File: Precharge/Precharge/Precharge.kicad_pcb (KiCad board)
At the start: 2 copper layers, 133 x 98 mm, 121 parts, among them J1 MicroFit, J2 Mini-Fit_Jr_5566-04A, J3 Micro-Fit 43045-0212, K1 OMRON-G2RL-24, K2 G7L-2A-X-L, Q1 2N7002, Q2 MMBT3906, Q3 2N7002, U1 TJA1051T-3, U10 LM393, U11 4N35, U2 SPAN02A-12, U3 Teensy4.0, U4 LM1117-5.0, U5 4N35, U6 4N35, U7 LM331, U8 LM331, U9 LM2904

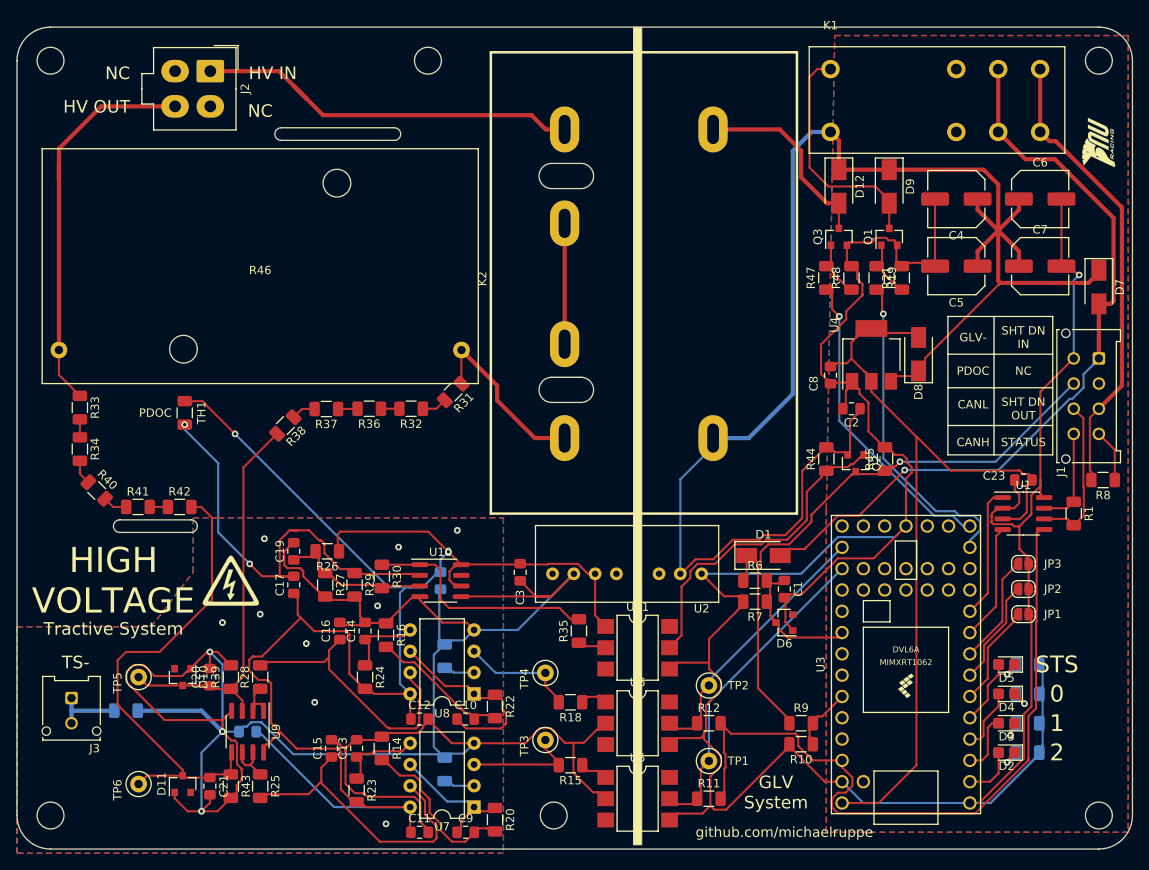
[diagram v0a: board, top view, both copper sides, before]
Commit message: :pencil: tidy-up pcb artwork
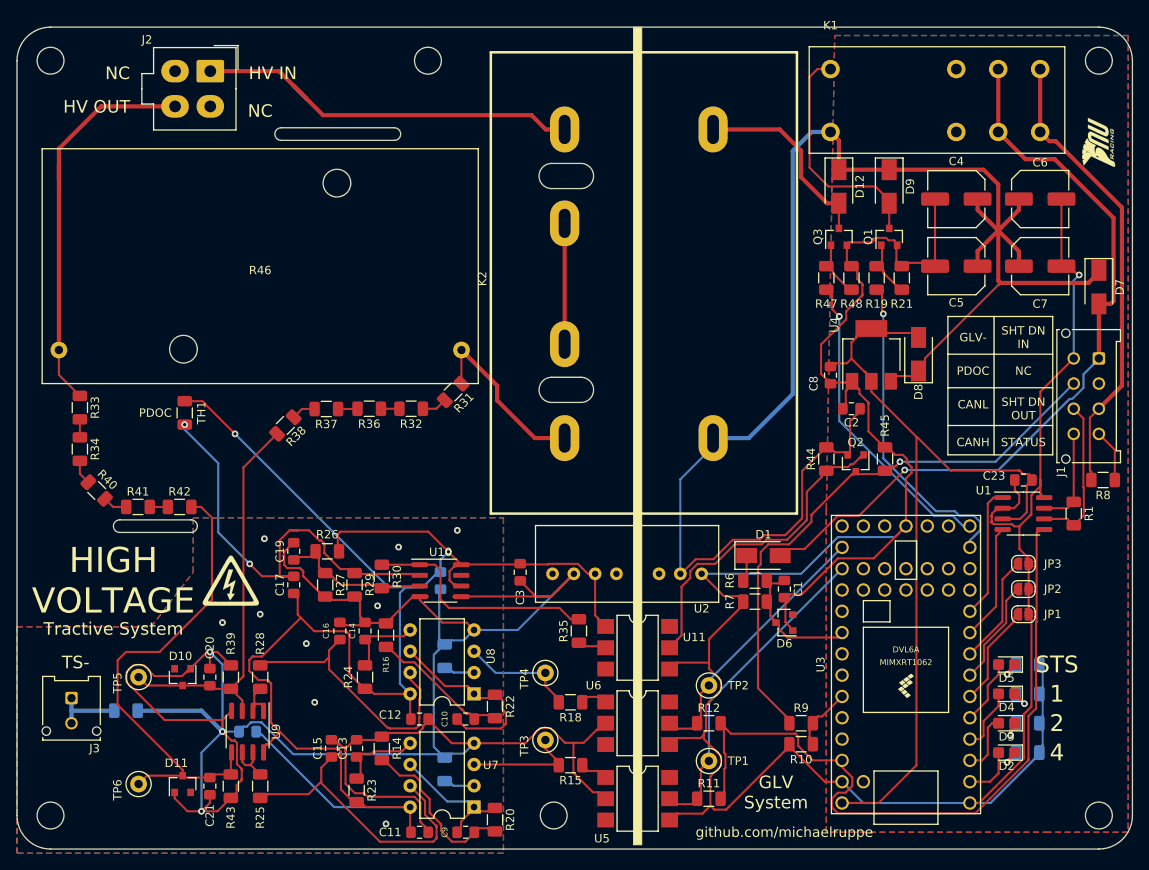
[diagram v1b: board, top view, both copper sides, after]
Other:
- board text added: "4"
- board text removed: "0"
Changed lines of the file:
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@@
       (outputformat 1)
       (mirror false)
-      (drillshape 1)
+      (drillshape 0)
       (scaleselection 1)
-      (outputdirectory ""))
+      (outputdirectory "C:/Users/Michael/Desktop/precharge-gerbers/"))
   )
   (net 0 "")
@@
     (descr "Molex Mini-Fit Jr. Power Connectors, old mpn/engineering number: 5566-04A, example for new mpn: 39-28-x04x, 2 Pins per row, Mounting:  (http://www.molex.com/pdm_docs/sd/039281043_sd.pdf), generated with kicad-footprint-generator")
     (tags "connector Molex Mini-Fit_Jr side entry")
-    (fp_text reference J2 (at 2.1 -3.45 90) (layer F.SilkS)
+    (fp_text reference J2 (at -3.75 8.25 180) (layer F.SilkS)
       (effects (font (size 1 1) (thickness 0.15)))
     )
@@
     (tags "SOIC SO")
     (attr smd)
-    (fp_text reference U1 (at 0 -3.4) (layer F.SilkS)
+    (fp_text reference U1 (at -4.75 -2.75) (layer F.SilkS)
       (effects (font (size 1 1) (thickness 0.15)))
     )
@@
     (tags "SMD DIP DIL PDIP SMDIP 2.54mm 7.62mm 300mil")
     (attr smd)
-    (fp_text reference U11 (at 0 -4.87) (layer F.SilkS)
+    (fp_text reference U11 (at 6.75 -1.25) (layer F.SilkS)
       (effects (font (size 1 1) (thickness 0.15)))
     )
@@
     (tags "SMD DIP DIL PDIP SMDIP 2.54mm 7.62mm 300mil")
     (attr smd)
-    (fp_text reference U6 (at 0 -4.87) (layer F.SilkS)
+    (fp_text reference U6 (at -5.25 -4.5) (layer F.SilkS)
       (effects (font (size 1 1) (thickness 0.15)))
     )
@@
     (tags "SMD DIP DIL PDIP SMDIP 2.54mm 7.62mm 300mil")
     (attr smd)
-    (fp_text reference U5 (at 0 -4.87) (layer F.SilkS)
+    (fp_text reference U5 (at -4.25 4.75) (layer F.SilkS)
       (effects (font (size 1 1) (thickness 0.15)))
     )
@@
     (descr "8-lead though-hole mounted DIP package, row spacing 7.62 mm (300 mils)")
     (tags "THT DIP DIL PDIP 2.54mm 7.62mm 300mil")
-    (fp_text reference U8 (at 3.81 -2.33) (layer F.SilkS)
+    (fp_text reference U8 (at -2 4.5 90) (layer F.SilkS)
       (effects (font (size 1 1) (thickness 0.15)))
     )
@@
     (descr "8-lead though-hole mounted DIP package, row spacing 7.62 mm (300 mils)")
     (tags "THT DIP DIL PDIP 2.54mm 7.62mm 300mil")
-    (fp_text reference U7 (at 3.81 -2.33) (layer F.SilkS)
+    (fp_text reference U7 (at -2 5) (layer F.SilkS)
       (effects (font (size 1 1) (thickness 0.15)))
     )
@@
     (tags resistor)
     (attr smd)
-    (fp_text reference R45 (at 0 -1.82 90) (layer F.SilkS)
+    (fp_text reference R45 (at 4 0 90) (layer F.SilkS)
       (effects (font (size 1 1) (thickness 0.15)))
     )
@@
     (tags resistor)
     (attr smd)
-    (fp_text reference R43 (at 0 -1.82 90) (layer F.SilkS)
+    (fp_text reference R43 (at 3.75 0 90) (layer F.SilkS)
       (effects (font (size 1 1) (thickness 0.15)))
     )
@@
     (tags resistor)
     (attr smd)
-    (fp_text reference R39 (at 0 -1.82 90) (layer F.SilkS)
+    (fp_text reference R39 (at 4 0 90) (layer F.SilkS)
       (effects (font (size 1 1) (thickness 0.15)))
     )
@@
     (tags resistor)
     (attr smd)
-    (fp_text reference R28 (at 0 -1.82 90) (layer F.SilkS)
+    (fp_text reference R28 (at 4 0 90) (layer F.SilkS)
       (effects (font (size 1 1) (thickness 0.15)))
     )
@@
     (tags resistor)
     (attr smd)
-    (fp_text reference R25 (at 0 -1.82 90) (layer F.SilkS)
+    (fp_text reference R25 (at 3.75 0 90) (layer F.SilkS)
       (effects (font (size 1 1) (thickness 0.15)))
     )
@@
     (tags resistor)
     (attr smd)
-    (fp_text reference R24 (at 0 -1.82 90) (layer F.SilkS)
+    (fp_text reference R24 (at 0 2 90) (layer F.SilkS)
       (effects (font (size 1 1) (thickness 0.15)))
     )
@@
     (tags resistor)
     (attr smd)
-    (fp_text reference R16 (at 0 -1.82 90) (layer F.SilkS)
-      (effects (font (size 1 1) (thickness 0.15)))
+    (fp_text reference R16 (at 3.5 0 90) (layer F.SilkS)
+      (effects (font (size 0.7 0.7) (thickness 0.15)))
     )
     (fp_text value 47 (at 0 1.82 90) (layer F.Fab)
@@
     (tags resistor)
     (attr smd)
-    (fp_text reference R7 (at 0 -1.82) (layer F.SilkS)
+    (fp_text reference R7 (at 3 0 90) (layer F.SilkS)
       (effects (font (size 1 1) (thickness 0.15)))
     )
@@
     (tags resistor)
     (attr smd)
-    (fp_text reference R6 (at 0 -1.82) (layer F.SilkS)
+    (fp_text reference R6 (at -3 0 90) (layer F.SilkS)
       (effects (font (size 1 1) (thickness 0.15)))
     )
@@
     (tags SOT-23)
     (attr smd)
-    (fp_text reference Q2 (at 0 -2.5 90) (layer F.SilkS)
+    (fp_text reference Q2 (at -2.5 0 180) (layer F.SilkS)
       (effects (font (size 1 1) (thickness 0.15)))
     )
@@
     (tags SOT-23)
     (attr smd)
-    (fp_text reference D11 (at 0 -2.5 90) (layer F.SilkS)
+    (fp_text reference D11 (at 2.5 -0.75 180) (layer F.SilkS)
       (effects (font (size 1 1) (thickness 0.15)))
     )
@@
     (tags SOT-23)
     (attr smd)
-    (fp_text reference D10 (at 0 -2.5 90) (layer F.SilkS)
+    (fp_text reference D10 (at -2.5 0.25 180) (layer F.SilkS)
       (effects (font (size 1 1) (thickness 0.15)))
     )
@@
     (tags "capacitor electrolyic nonpolar")
     (attr smd)
-    (fp_text reference C7 (at 0 -4.35) (layer F.SilkS)
+    (fp_text reference C7 (at 0 4.5) (layer F.SilkS)
       (effects (font (size 1 1) (thickness 0.15)))
     )
@@
     (tags "capacitor handsolder")
     (attr smd)
-    (fp_text reference C21 (at 0 -1.65 90) (layer F.SilkS)
+    (fp_text reference C21 (at 3.5 0 90) (layer F.SilkS)
       (effects (font (size 1 1) (thickness 0.15)))
     )
@@
     (tags "capacitor handsolder")
     (attr smd)
-    (fp_text reference C20 (at 0 -1.65 90) (layer F.SilkS)
+    (fp_text reference C20 (at 3.5 0 90) (layer F.SilkS)
       (effects (font (size 1 1) (thickness 0.15)))
     )
@@
     (attr smd)
     (fp_text reference C16 (at 0 -1.65 90) (layer F.SilkS)
-      (effects (font (size 1 1) (thickness 0.15)))
+      (effects (font (size 0.7 0.7) (thickness 0.15)))
     )
     (fp_text value 100n (at 0 1.65 90) (layer F.Fab)
@@
     (tags "capacitor handsolder")
     (attr smd)
-    (fp_text reference C14 (at 0 -1.65 90) (layer F.SilkS)
-      (effects (font (size 1 1) (thickness 0.15)))
+    (fp_text reference C14 (at 0 -1.5 90) (layer F.SilkS)
+      (effects (font (size 0.7 0.7) (thickness 0.15)))
     )
     (fp_text value 10n (at 0 1.65 90) (layer F.Fab)
@@
     (tags "capacitor handsolder")
     (attr smd)
-    (fp_text reference C12 (at 0 -1.65) (layer F.SilkS)
+    (fp_text reference C12 (at -3.5 -0.5) (layer F.SilkS)
       (effects (font (size 1 1) (thickness 0.15)))
     )
@@
     (tags "capacitor handsolder")
     (attr smd)
-    (fp_text reference C11 (at 0 -1.65) (layer F.SilkS)
+    (fp_text reference C11 (at -3.5 0) (layer F.SilkS)
       (effects (font (size 1 1) (thickness 0.15)))
     )
@@
     (tags "capacitor handsolder")
     (attr smd)
-    (fp_text reference C10 (at 0 -1.65) (layer F.SilkS)
-      (effects (font (size 1 1) (thickness 0.15)))
+    (fp_text reference C10 (at -2.5 0 90) (layer F.SilkS)
+      (effects (font (size 0.7 0.7) (thickness 0.15)))
     )
     (fp_text value 1u (at 0 1.65) (layer F.Fab)
@@
     (tags "capacitor handsolder")
     (attr smd)
-    (fp_text reference C9 (at 0 -1.65) (layer F.SilkS)
-      (effects (font (size 1 1) (thickness 0.15)))
+    (fp_text reference C9 (at -2.5 0 90) (layer F.SilkS)
+      (effects (font (size 0.7 0.7) (thickness 0.15)))
     )
     (fp_text value 1u (at 0 1.65) (layer F.Fab)
@@
     (tags resistor)
     (attr smd)
-    (fp_text reference R48 (at 0 -1.82 90) (layer F.SilkS)
+    (fp_text reference R48 (at -3.1 0 180) (layer F.SilkS)
       (effects (font (size 1 1) (thickness 0.15)))
     )
@@
     (tags resistor)
     (attr smd)
-    (fp_text reference R47 (at 0 -1.82 90) (layer F.SilkS)
+    (fp_text reference R47 (at -3.1 0 180) (layer F.SilkS)
       (effects (font (size 1 1) (thickness 0.15)))
     )
@@
     (tags resistor)
     (attr smd)
-    (fp_text reference R26 (at 0 -1.82) (layer F.SilkS)
+    (fp_text reference R26 (at 0 2) (layer F.SilkS)
       (effects (font (size 1 1) (thickness 0.15)))
     )
@@
     (tags resistor)
     (attr smd)
-    (fp_text reference R21 (at 0 -1.82 90) (layer F.SilkS)
+    (fp_text reference R21 (at -3.1 0 180) (layer F.SilkS)
       (effects (font (size 1 1) (thickness 0.15)))
     )
@@
     (tags resistor)
     (attr smd)
-    (fp_text reference R19 (at 0 -1.82 90) (layer F.SilkS)
+    (fp_text reference R19 (at 3.1 0 180) (layer F.SilkS)
       (effects (font (size 1 1) (thickness 0.15)))
     )
@@
     (tags "capacitor electrolyic nonpolar")
     (attr smd)
-    (fp_text reference C4 (at 0 -4.35) (layer F.SilkS)
+    (fp_text reference C4 (at 0 4.5) (layer F.SilkS)
       (effects (font (size 1 1) (thickness 0.15)))
     )
@@
     )
   )
-  (gr_text 2 (at 192 137) (layer F.SilkS)
+  (gr_text 4 (at 192 137) (layer F.SilkS)
     (effects (font (size 2 2) (thickness 0.3)))
   )
-  (gr_text 1 (at 192 133.5) (layer F.SilkS)
+  (gr_text 2 (at 192 133.5) (layer F.SilkS)
     (effects (font (size 2 2) (thickness 0.3)))
   )
-  (gr_text 0 (at 192 130) (layer F.SilkS)
+  (gr_text 1 (at 192 130) (layer F.SilkS)
     (effects (font (size 2 2) (thickness 0.3)))
   )
